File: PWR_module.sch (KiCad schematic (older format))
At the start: 44 parts, among them J1 CONN_01X01, J2 CONN_01X01, J3 CONN_01X01, Q1 BS250, U1 VTX-214-020-115, U2 RT7297BHZSP, U3 RT7297BHZSP

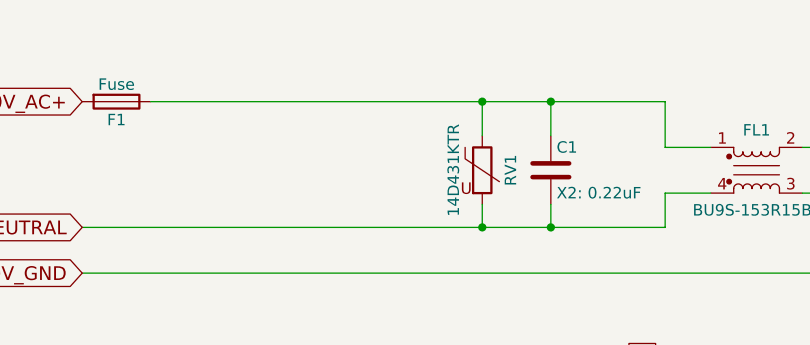
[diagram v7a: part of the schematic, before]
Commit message: the fuse is now protecting the ssr circle too, not just the ac-dc
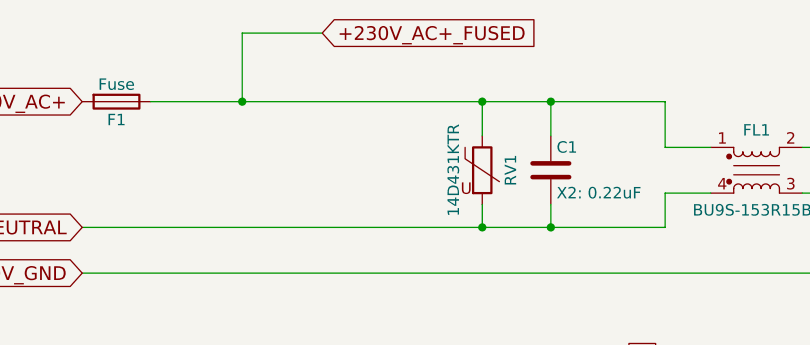
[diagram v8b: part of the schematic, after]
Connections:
- net +230V_AC+_FUSED: now reaches C1.1, F1.1, FL1.1, RV1.1
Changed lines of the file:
@@
 Wire Wire Line
 	6300 3250 8200 3250
+Text GLabel 2400 750  2    60   Input ~ 0
++230V_AC+_FUSED
+Wire Wire Line
+	2050 1050 2050 750
+Wire Wire Line
+	2050 750  2400 750
+Connection ~ 2050 1050
 $EndSCHEMATC
